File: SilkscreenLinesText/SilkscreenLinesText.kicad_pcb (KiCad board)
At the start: 2 copper layers, 100 x 100 mm, 16 parts

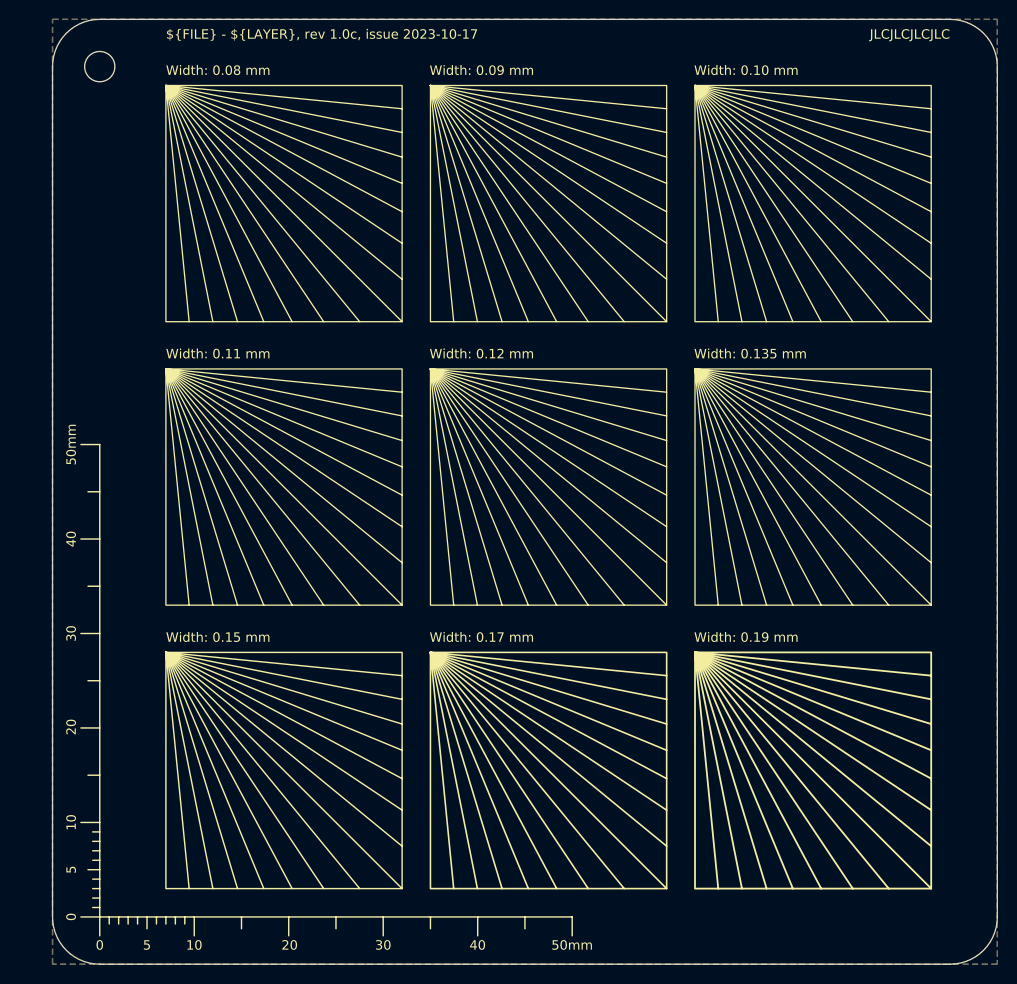
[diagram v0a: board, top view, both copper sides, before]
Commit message: Added project footprint library
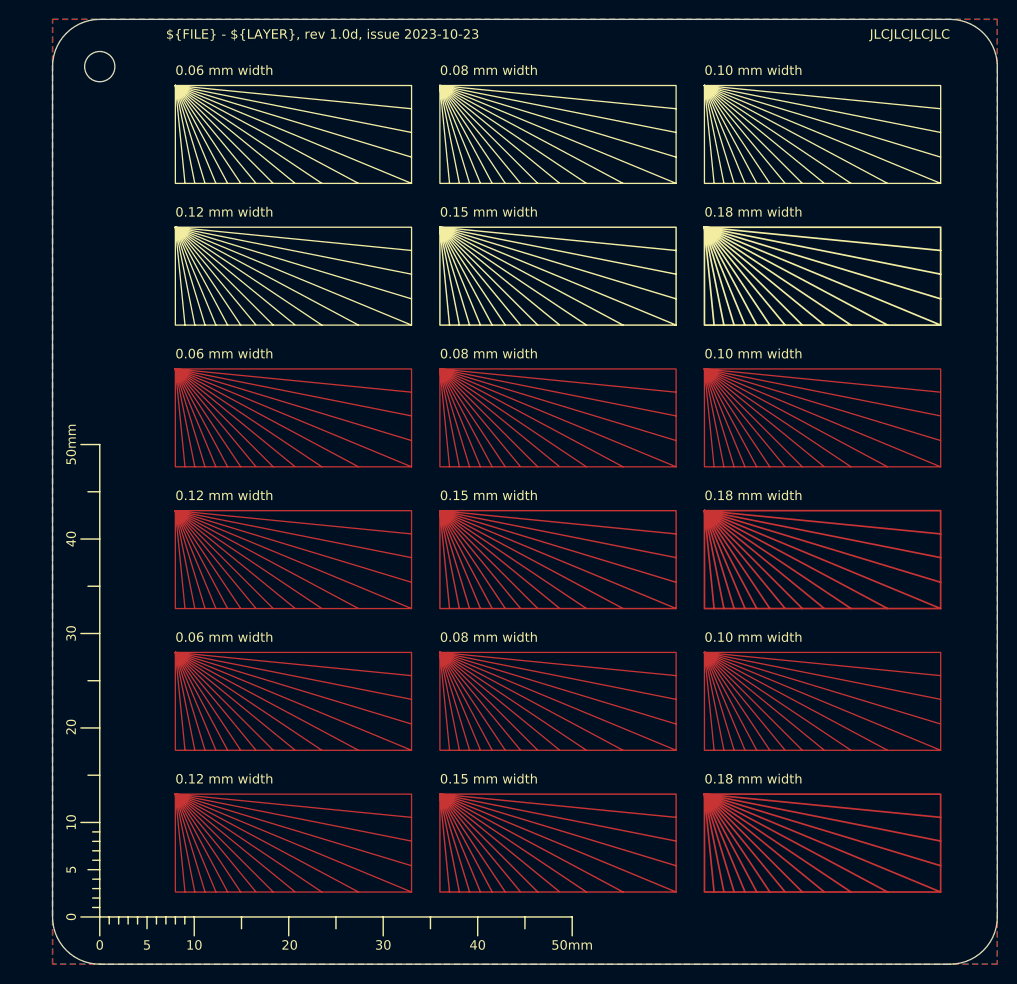
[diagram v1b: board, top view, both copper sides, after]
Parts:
- removed the ~ at (119.3, 43.2)
- removed the ~ at (63.3, 73.2)
- removed the ~ at (63.3, 103.2)
- removed the ~ at (119.3, 73.2)
- removed the ~ at (119.3, 103.2)
- removed the ~ at (63.3, 43.2)
- removed the ~ at (91.3, 73.2)
- removed the ~ at (91.3, 43.2)
- removed the ~ at (91.3, 103.2)
- added ~: 0.06 mm width, SilkScreenTests:Silkscreen_Lines_25x10mm_0.15mm, F.Cu at (64.3, 43.2)
- added ~: 0.15 mm width, SilkScreenTests:Lines_Copper_25x10mm_0.15mm, F.Cu at (92.3, 118.2)
- added ~: 0.10 mm width, SilkScreenTests:Lines_Copper_25x10mm_0.15mm, F.Cu at (120.3, 73.2)
- added ~: 0.10 mm width, SilkScreenTests:Lines_Copper_25x10mm_0.15mm, F.Cu at (120.3, 103.2)
- added ~: 0.12 mm width, SilkScreenTests:Lines_Copper_25x10mm_0.15mm, F.Cu at (64.3, 88.2)
- added ~: 0.08 mm width, SilkScreenTests:Silkscreen_Lines_25x10mm_0.15mm, F.Cu at (92.3, 43.2)
- added ~: 0.06 mm width, SilkScreenTests:Lines_Copper_25x10mm_0.15mm, F.Cu at (64.3, 73.2)
- added ~: 0.10 mm width, SilkScreenTests:Silkscreen_Lines_25x10mm_0.15mm, F.Cu at (120.3, 43.2)
- added ~: 0.08 mm width, SilkScreenTests:Lines_Copper_25x10mm_0.15mm, F.Cu at (92.3, 73.2)
- added ~: 0.18 mm width, SilkScreenTests:Silkscreen_Lines_25x10mm_0.15mm, F.Cu at (120.3, 58.2)
- added ~: 0.06 mm width, SilkScreenTests:Lines_Copper_25x10mm_0.15mm, F.Cu at (64.3, 103.2)
- added ~: 0.08 mm width, SilkScreenTests:Lines_Copper_25x10mm_0.15mm, F.Cu at (92.3, 103.2)
- added ~: 0.18 mm width, SilkScreenTests:Lines_Copper_25x10mm_0.15mm, F.Cu at (120.3, 118.2)
- added ~: 0.12 mm width, SilkScreenTests:Lines_Copper_25x10mm_0.15mm, F.Cu at (64.3, 118.2)
- added ~: 0.15 mm width, SilkScreenTests:Silkscreen_Lines_25x10mm_0.15mm, F.Cu at (92.3, 58.2)
- added ~: 0.15 mm width, SilkScreenTests:Lines_Copper_25x10mm_0.15mm, F.Cu at (92.3, 88.2)
- added ~: 0.18 mm width, SilkScreenTests:Lines_Copper_25x10mm_0.15mm, F.Cu at (120.3, 88.2)
- added ~: 0.12 mm width, SilkScreenTests:Silkscreen_Lines_25x10mm_0.15mm, F.Cu at (64.3, 58.2)
- ~: footprint SilkScreenTests:Silkscreen_Texts_SIZE_x_x_0.15 -> SilkScreenTests:Texts_Silkscreen_SIZE_x_x_0.15
- moved ~ 5.00 mm to (136.3, 44.2)

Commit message: Changed layout of pass/fail elements
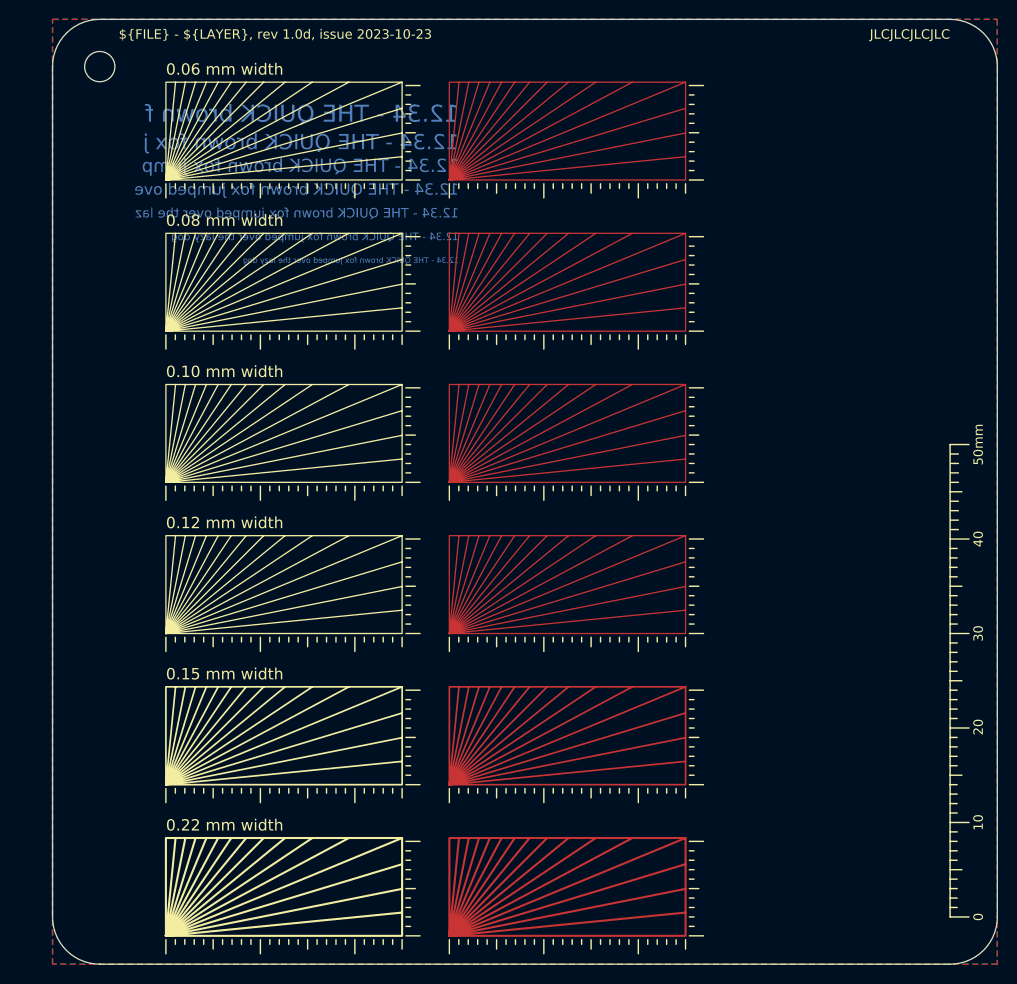
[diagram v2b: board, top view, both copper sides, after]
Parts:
- removed the REF** at (56.3, 131.2)
- removed the ~ at (64.3, 43.2)
- removed the ~ at (92.3, 118.2)
- removed the ~ at (120.3, 73.2)
- removed the ~ at (120.3, 103.2)
- removed the ~ at (64.3, 88.2)
- removed the ~ at (92.3, 43.2)
- removed the ~ at (64.3, 73.2)
- removed the ~ at (120.3, 43.2)
- removed the ~ at (92.3, 73.2)
- removed the ~ at (120.3, 58.2)
- removed the ~ at (131.3, 106.2)
- removed the ~ at (64.3, 103.2)
- removed the ~ at (136.3, 44.2)
- removed the ~ at (131.3, 75.2)
- removed the ~ at (92.3, 103.2)
- removed the ~ at (120.3, 118.2)
- removed the ~ at (64.3, 118.2)
- removed the ~ at (92.3, 58.2)
- removed the ~ at (92.3, 88.2)
- removed the ~ at (120.3, 88.2)
- removed the ~ at (64.3, 58.2)
- added REF**: Gauge_50mm_Type2_SilkScreenTop_FIXED, SilkScreenTests:Gauge_50mm_Type2_SilkScreenTop_FIXED, F.Cu at (146.3, 131.2)
- added ~: 0.10 mm width, SilkScreenTests:Lines_Silk+Cu_25x10mm_0.1mm, F.Cu at (63.3, 85.2)
- added ~: 0.15 mm width, SilkScreenTests:Lines_Silk+Cu_25x10mm_0.1mm, F.Cu at (63.3, 117.2)
- added ~: 0.08 mm width, SilkScreenTests:Lines_Silk+Cu_25x10mm_0.1mm, F.Cu at (63.3, 69.2)
- added ~: 0.22 mm width, SilkScreenTests:Lines_Silk+Cu_25x10mm_0.1mm, F.Cu at (63.3, 133.2)
- added ~: 0.12 mm width, SilkScreenTests:Lines_Silk+Cu_25x10mm_0.1mm, F.Cu at (63.3, 101.2)
- added ~: 0.06 mm width, SilkScreenTests:Lines_Silk+Cu_25x10mm_0.1mm, F.Cu at (63.3, 53.2)
- added ~: SIZE (h/w/t): x/x/0.15x, SilkScreenTests:Texts_Silk+Cu_SIZE_x_x_0.15, B.Cu at (136.3, 44.2)
